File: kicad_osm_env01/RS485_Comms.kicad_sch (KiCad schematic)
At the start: 17 parts

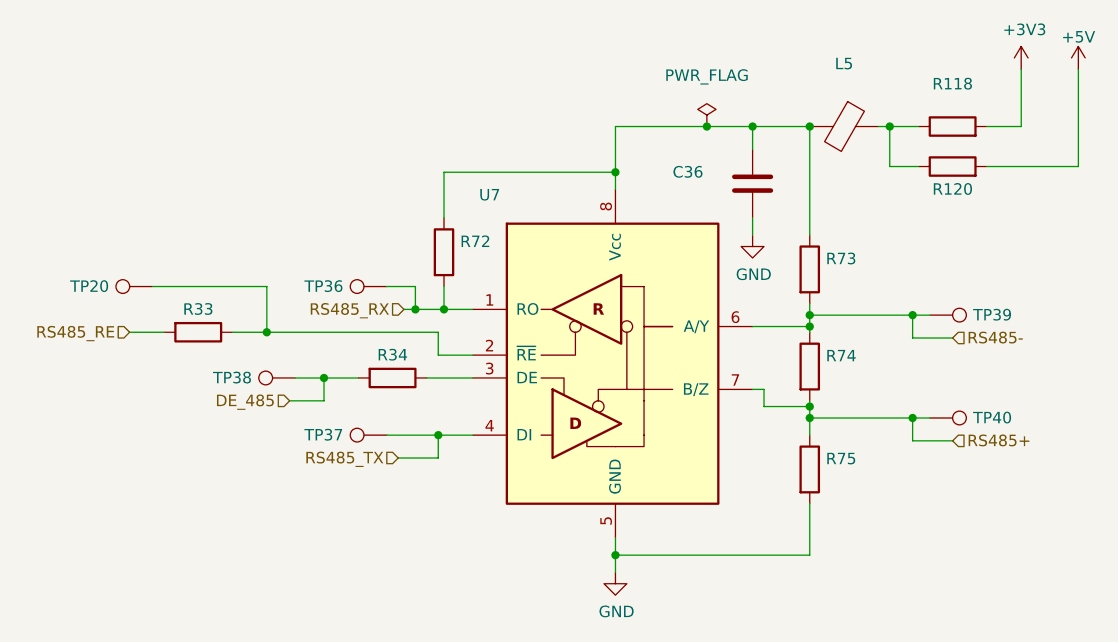
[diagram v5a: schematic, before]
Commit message: majority of signals routed on layout
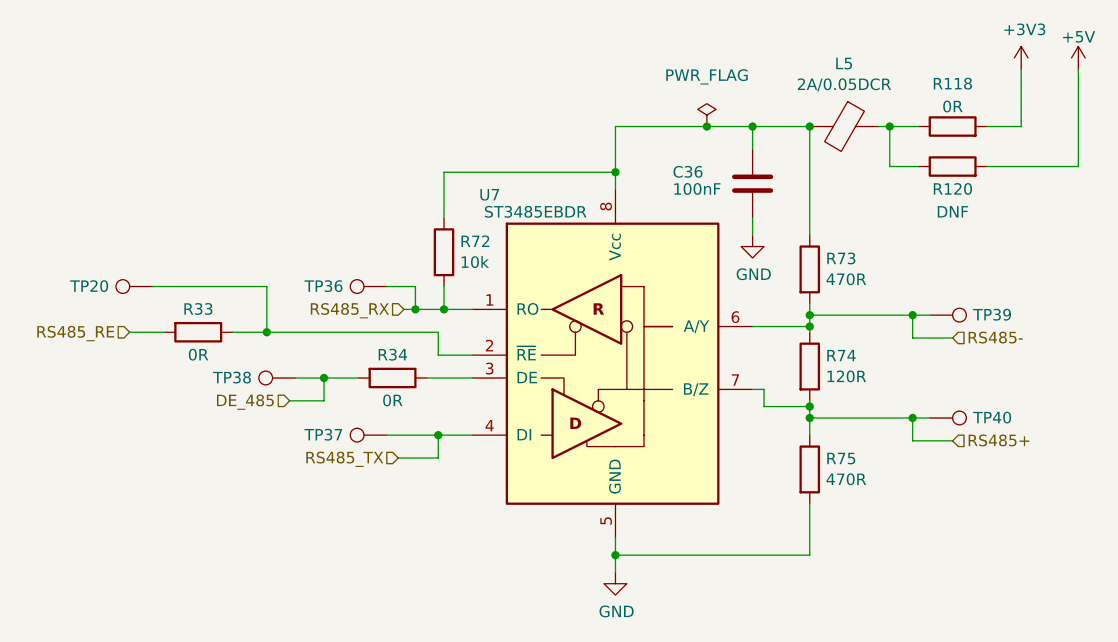
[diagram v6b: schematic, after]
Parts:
- C36: value (none) -> 100nF; footprint (none) -> Capacitor_SMD:C_0402_1005Metric
- L5: value (none) -> 2A/0.05DCR; footprint (none) -> Inductor_SMD:L_0402_1005Metric
- R118, R33, R34: value (none) -> 0R; footprint (none) -> Resistor_SMD:R_0603_1608Metric
- R120: value (none) -> DNF; footprint (none) -> Resistor_SMD:R_0603_1608Metric
- R72: value (none) -> 10k; footprint (none) -> Resistor_SMD:R_0603_1608Metric
- R73, R75: value (none) -> 470R; footprint (none) -> Resistor_SMD:R_0603_1608Metric
- R74: value (none) -> 120R; footprint (none) -> Resistor_SMD:R_0603_1608Metric
- TP20, TP36, TP37, TP38, TP39, TP40: value (none) -> Test_Point; footprint (none) -> TestPoint:TestPoint_THTPad_D1.0mm_Drill0.5mm
- U7: value (none) -> ST3485EBDR; footprint (none) -> Package_SO:SOIC-8_3.9x4.9mm_P1.27mm
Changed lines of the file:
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@@
     (in_bom yes) (on_board yes)
     (property "Reference" "U7" (id 0) (at 129.54 79.375 0))
-    (property "Value" "" (id 1) (at 134.62 81.28 0))
-    (property "Footprint" "" (id 2) (at 140.335 99.695 0)
+    (property "Value" "ST3485EBDR" (id 1) (at 134.62 81.28 0))
+    (property "Footprint" "Package_SO:SOIC-8_3.9x4.9mm_P1.27mm" (id 2) (at 140.335 99.695 0)
       (effects (font (size 1.27 1.27) italic) hide)
     )
@@
       (effects (font (size 1.27 1.27)) (justify left))
     )
-    (property "Value" "" (id 1) (at 149.86 78.74 0)
-      (effects (font (size 1.27 1.27)) (justify left))
-    )
-    (property "Footprint" "" (id 2) (at 159.7152 81.915 0)
+    (property "Value" "100nF" (id 1) (at 149.86 78.74 0)
+      (effects (font (size 1.27 1.27)) (justify left))
+    )
+    (property "Footprint" "Capacitor_SMD:C_0402_1005Metric" (id 2) (at 159.7152 81.915 0)
       (effects (font (size 1.27 1.27)) hide)
     )
@@
       (effects (font (size 1.27 1.27)) (justify left))
     )
-    (property "Value" "" (id 1) (at 126.238 86.868 0)
-      (effects (font (size 1.27 1.27)) (justify left))
-    )
-    (property "Footprint" "" (id 2) (at 122.682 85.725 90)
+    (property "Value" "10k" (id 1) (at 126.238 86.868 0)
+      (effects (font (size 1.27 1.27)) (justify left))
+    )
+    (property "Footprint" "Resistor_SMD:R_0603_1608Metric" (id 2) (at 122.682 85.725 90)
       (effects (font (size 1.27 1.27)) hide)
     )
@@
       (effects (font (size 1.27 1.27)) (justify left))
     )
-    (property "Value" "" (id 1) (at 166.878 88.773 0)
-      (effects (font (size 1.27 1.27)) (justify left))
-    )
-    (property "Footprint" "" (id 2) (at 163.322 87.63 90)
+    (property "Value" "470R" (id 1) (at 166.878 88.773 0)
+      (effects (font (size 1.27 1.27)) (justify left))
+    )
+    (property "Footprint" "Resistor_SMD:R_0603_1608Metric" (id 2) (at 163.322 87.63 90)
       (effects (font (size 1.27 1.27)) hide)
     )
@@
       (effects (font (size 1.27 1.27)) (justify left))
     )
-    (property "Value" "" (id 1) (at 166.878 99.568 0)
-      (effects (font (size 1.27 1.27)) (justify left))
-    )
-    (property "Footprint" "" (id 2) (at 163.322 98.425 90)
+    (property "Value" "120R" (id 1) (at 166.878 99.568 0)
+      (effects (font (size 1.27 1.27)) (justify left))
+    )
+    (property "Footprint" "Resistor_SMD:R_0603_1608Metric" (id 2) (at 163.322 98.425 90)
       (effects (font (size 1.27 1.27)) hide)
     )
@@
       (effects (font (size 1.27 1.27)) (justify left))
     )
-    (property "Value" "" (id 1) (at 166.878 110.998 0)
-      (effects (font (size 1.27 1.27)) (justify left))
-    )
-    (property "Footprint" "" (id 2) (at 163.322 109.855 90)
+    (property "Value" "470R" (id 1) (at 166.878 110.998 0)
+      (effects (font (size 1.27 1.27)) (justify left))
+    )
+    (property "Footprint" "Resistor_SMD:R_0603_1608Metric" (id 2) (at 163.322 109.855 90)
       (effects (font (size 1.27 1.27)) hide)
     )
@@
     (in_bom yes) (on_board yes)
     (property "Reference" "TP39" (id 0) (at 185.42 92.71 90))
-    (property "Value" "" (id 1) (at 187.96 92.71 90)
-      (effects (font (size 1.27 1.27)) hide)
-    )
-    (property "Footprint" "" (id 2) (at 178.435 97.79 0)
+    (property "Value" "Test_Point" (id 1) (at 187.96 92.71 90)
+      (effects (font (size 1.27 1.27)) hide)
+    )
+    (property "Footprint" "TestPoint:TestPoint_THTPad_D1.0mm_Drill0.5mm" (id 2) (at 178.435 97.79 0)
       (effects (font (size 1.27 1.27)) hide)
     )
@@
     (in_bom yes) (on_board yes)
     (property "Reference" "TP40" (id 0) (at 185.42 104.14 90))
-    (property "Value" "" (id 1) (at 187.96 104.14 90)
-      (effects (font (size 1.27 1.27)) hide)
-    )
-    (property "Footprint" "" (id 2) (at 178.435 109.22 0)
+    (property "Value" "Test_Point" (id 1) (at 187.96 104.14 90)
+      (effects (font (size 1.27 1.27)) hide)
+    )
+    (property "Footprint" "TestPoint:TestPoint_THTPad_D1.0mm_Drill0.5mm" (id 2) (at 178.435 109.22 0)
       (effects (font (size 1.27 1.27)) hide)
     )
@@
     (in_bom yes) (on_board yes)
     (property "Reference" "TP38" (id 0) (at 100.965 99.695 90))
-    (property "Value" "" (id 1) (at 98.425 101.6 90)
-      (effects (font (size 1.27 1.27)) hide)
-    )
-    (property "Footprint" "" (id 2) (at 107.95 94.615 0)
+    (property "Value" "Test_Point" (id 1) (at 98.425 101.6 90)
+      (effects (font (size 1.27 1.27)) hide)
+    )
+    (property "Footprint" "TestPoint:TestPoint_THTPad_D1.0mm_Drill0.5mm" (id 2) (at 107.95 94.615 0)
       (effects (font (size 1.27 1.27)) hide)
     )
@@
     (in_bom yes) (on_board yes)
     (property "Reference" "TP37" (id 0) (at 111.125 106.045 90))
-    (property "Value" "" (id 1) (at 108.585 107.95 90)
-      (effects (font (size 1.27 1.27)) hide)
-    )
-    (property "Footprint" "" (id 2) (at 118.11 100.965 0)
+    (property "Value" "Test_Point" (id 1) (at 108.585 107.95 90)
+      (effects (font (size 1.27 1.27)) hide)
+    )
+    (property "Footprint" "TestPoint:TestPoint_THTPad_D1.0mm_Drill0.5mm" (id 2) (at 118.11 100.965 0)
       (effects (font (size 1.27 1.27)) hide)
     )
@@
     (in_bom yes) (on_board yes)
     (property "Reference" "TP36" (id 0) (at 111.125 89.535 90))
-    (property "Value" "" (id 1) (at 108.585 86.36 90)
-      (effects (font (size 1.27 1.27)) hide)
-    )
-    (property "Footprint" "" (id 2) (at 118.11 84.455 0)
+    (property "Value" "Test_Point" (id 1) (at 108.585 86.36 90)
+      (effects (font (size 1.27 1.27)) hide)
+    )
+    (property "Footprint" "TestPoint:TestPoint_THTPad_D1.0mm_Drill0.5mm" (id 2) (at 118.11 84.455 0)
       (effects (font (size 1.27 1.27)) hide)
     )
@@
     (in_bom yes) (on_board yes)
     (property "Reference" "R34" (id 0) (at 118.745 97.155 90))
-    (property "Value" "" (id 1) (at 118.745 102.235 90))
-    (property "Footprint" "" (id 2) (at 118.745 97.917 90)
+    (property "Value" "0R" (id 1) (at 118.745 102.235 90))
+    (property "Footprint" "Resistor_SMD:R_0603_1608Metric" (id 2) (at 118.745 97.917 90)
       (effects (font (size 1.27 1.27)) hide)
     )
@@
     (in_bom yes) (on_board yes)
     (property "Reference" "R33" (id 0) (at 97.155 92.075 90))
-    (property "Value" "" (id 1) (at 97.155 97.155 90))
-    (property "Footprint" "" (id 2) (at 97.155 92.837 90)
+    (property "Value" "0R" (id 1) (at 97.155 97.155 90))
+    (property "Footprint" "Resistor_SMD:R_0603_1608Metric" (id 2) (at 97.155 92.837 90)
       (effects (font (size 1.27 1.27)) hide)
     )
@@
     (in_bom yes) (on_board yes)
     (property "Reference" "L5" (id 0) (at 168.91 64.7954 90))
-    (property "Value" "" (id 1) (at 168.91 67.1068 90))
-    (property "Footprint" "" (id 2) (at 168.91 69.977 90)
+    (property "Value" "2A/0.05DCR" (id 1) (at 168.91 67.1068 90))
+    (property "Footprint" "Inductor_SMD:L_0402_1005Metric" (id 2) (at 168.91 69.977 90)
       (effects (font (size 1.27 1.27)) hide)
     )
@@
     (in_bom yes) (on_board yes)
     (property "Reference" "TP20" (id 0) (at 85.09 89.535 90))
-    (property "Value" "" (id 1) (at 82.55 86.36 90)
-      (effects (font (size 1.27 1.27)) hide)
-    )
-    (property "Footprint" "" (id 2) (at 92.075 84.455 0)
+    (property "Value" "Test_Point" (id 1) (at 82.55 86.36 90)
+      (effects (font (size 1.27 1.27)) hide)
+    )
+    (property "Footprint" "TestPoint:TestPoint_THTPad_D1.0mm_Drill0.5mm" (id 2) (at 92.075 84.455 0)
       (effects (font (size 1.27 1.27)) hide)
     )
@@
     (in_bom yes) (on_board yes)
     (property "Reference" "R120" (id 0) (at 180.975 78.74 90))
-    (property "Value" "" (id 1) (at 180.975 81.28 90))
-    (property "Footprint" "" (id 2) (at 180.975 77.978 90)
+    (property "Value" "DNF" (id 1) (at 180.975 81.28 90))
+    (property "Footprint" "Resistor_SMD:R_0603_1608Metric" (id 2) (at 180.975 77.978 90)
       (effects (font (size 1.27 1.27)) hide)
     )
@@
     (in_bom yes) (on_board yes) (fields_autoplaced)
     (property "Reference" "R118" (id 0) (at 180.975 67.0392 90))
-    (property "Value" "" (id 1) (at 180.975 69.5761 90))
-    (property "Footprint" "" (id 2) (at 180.975 73.533 90)
-      (effects (font (size 1.27 1.27)) hide)
-    )
+    (property "Value" "0R" (id 1) (at 180.975 69.5761 90))
+    (property "Footprint" "Resistor_SMD:R_0603_1608Metric" (id 2) (at 180.975 73.533 90)
+      (effects (font (size 1.27 1.27)) hide)
+    )
